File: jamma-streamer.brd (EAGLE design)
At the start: 180.3 x 92 mm, 63 parts, among them IC1 LM7805, J1 Audio line out, J2 ICSP, J3 SDCARD, J4 USB, T1 TY-145P, T2 TY-145P, U1 CD74HC165MD16-M, U10 LM358DTD8-M, U2 ATMEGA328PB-AUR, U3 74HC4050D, U4 TLV757X / LP298X, U5 CD74HC165MD16-M, U6 CD74HC165MD16-M, U7 FT232RL, U8 DS3231SNT&R21-0042B_16-M, U9 NDT2955SOT-223-M, Y1 16MHz

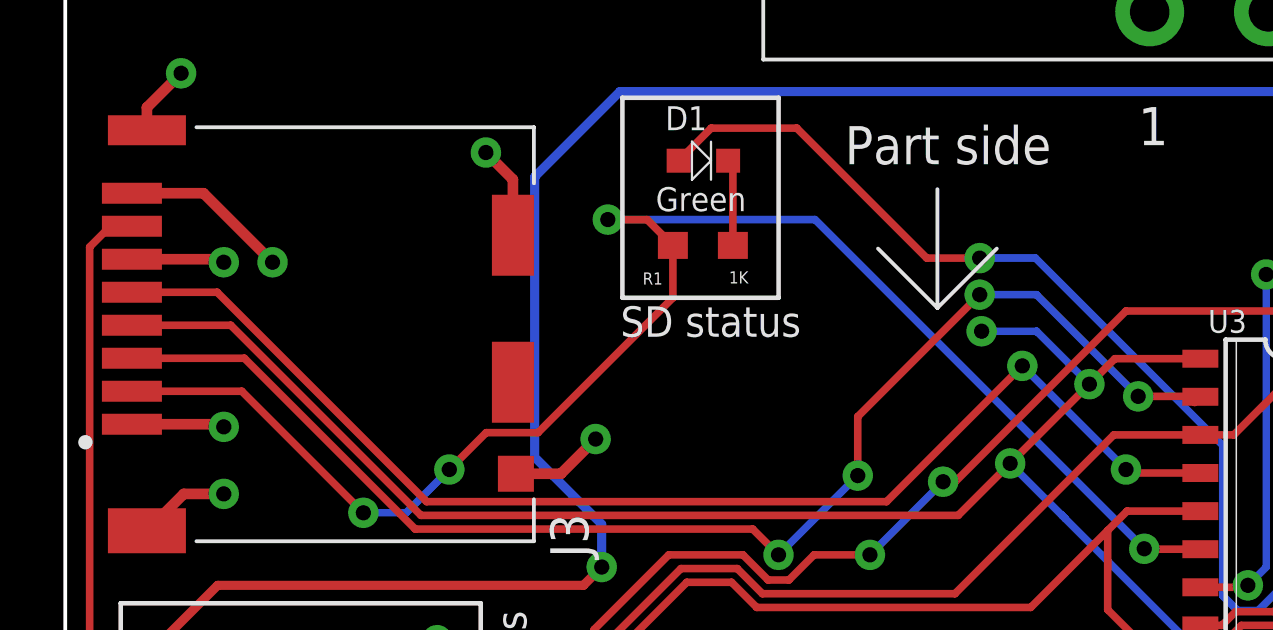
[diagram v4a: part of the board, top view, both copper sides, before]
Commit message: Added Arduino pinout diagram
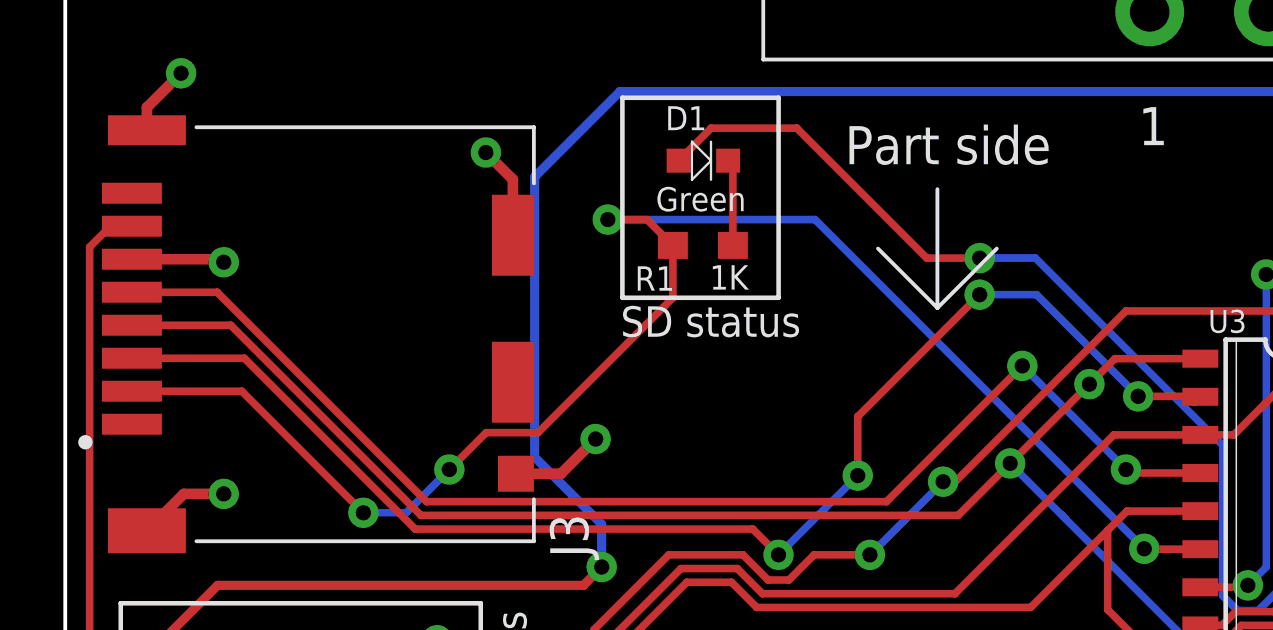
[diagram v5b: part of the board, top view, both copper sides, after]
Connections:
- net N$14 renamed SD_CS
- net N$15 renamed SD_CMD
- net N$17 renamed SD_CLK
- net GND: no longer J3.1, J3.8
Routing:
- net GND: track 221.8 -> 213.0 mm, vias 49 -> 47
- net VCC_2: track 77.9 -> 73.6 mm, vias 6 -> 5
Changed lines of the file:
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@@
 </element>
 <element name="R1" library="CMS" package="652-CHP0603FX1001ELF" value="1K" x="21.25375" y="76.76125" smashed="yes" rot="R180">
-<attribute name="NAME" x="19.91375" y="75.86125" size="0.4064" layer="21" rot="R180"/>
-<attribute name="VALUE" x="22.77125" y="75.8975" size="0.4064" layer="21" rot="R180"/>
+<attribute name="NAME" x="20.32015" y="76.06445" size="0.8128" layer="21" rot="R180"/>
+<attribute name="VALUE" x="22.77125" y="76.1007" size="0.8128" layer="21" rot="R180"/>
 </element>
 <element name="D1" library="CMS" package="604-APTD1608LCGCK" value="Green" x="21.27" y="79.585" smashed="yes">
@@
 </polygon>
 </signal>
-<signal name="GND">
+<signal name="GND" airwireshidden="yes">
 <contactref element="JAMMA_IN" pad="_F"/>
 <contactref element="JAMMA_OUT_BTM" pad="_F"/>
@@
 <contactref element="J3" pad="S2"/>
 <contactref element="J3" pad="6"/>
-<contactref element="J3" pad="8"/>
-<contactref element="J3" pad="1"/>
 <contactref element="U3" pad="8"/>
 <contactref element="U3" pad="11"/>
@@
 <wire x1="3.94965" y1="68.4784" x2="5.2832" y2="68.4784" width="0.3556" layer="1"/>
 <via x="5.2832" y="68.4784" extent="1-16" drill="0.508"/>
-<wire x1="2.22125" y1="70.8" x2="5.1968" y2="70.8" width="0.3556" layer="1"/>
-<wire x1="5.1968" y1="70.8" x2="5.2832" y2="70.7136" width="0.3556" layer="1"/>
-<via x="5.2832" y="70.7136" extent="1-16" drill="0.508"/>
 <wire x1="2.22125" y1="76.3" x2="5.1832" y2="76.3" width="0.3556" layer="1"/>
 <wire x1="5.1832" y1="76.3" x2="5.2832" y2="76.2" width="0.3556" layer="1"/>
 <via x="5.2832" y="76.2" extent="1-16" drill="0.508"/>
-<wire x1="2.22125" y1="78.5" x2="4.6088" y2="78.5" width="0.3556" layer="1"/>
-<wire x1="4.6088" y1="78.5" x2="6.9088" y2="76.2" width="0.3556" layer="1"/>
-<via x="6.9088" y="76.2" extent="1-16" drill="0.508"/>
 <wire x1="2.72125" y1="80.6" x2="2.72125" y2="81.35965" width="0.3556" layer="1"/>
 <wire x1="2.72125" y1="81.35965" x2="3.8608" y2="82.4992" width="0.3556" layer="1"/>
@@
 <wire x1="11.1252" y1="50.7492" x2="9.5504" y2="49.1744" width="0.254" layer="1"/>
 </signal>
-<signal name="N$15">
+<signal name="SD_CMD">
 <contactref element="U3" pad="2"/>
 <contactref element="J3" pad="3"/>
@@
 <wire x1="22.2102375" y1="65.532" x2="20.716625" y2="65.532" width="0.254" layer="1"/>
 </signal>
-<signal name="N$17">
+<signal name="SD_CLK">
 <contactref element="U3" pad="4"/>
 <contactref element="J3" pad="5"/>
@@
 <wire x1="12.0442" y1="68.2198" x2="27.3766" y2="68.2198" width="0.254" layer="1"/>
 </signal>
-<signal name="N$14">
+<signal name="SD_CS">
 <contactref element="J3" pad="2"/>
 <contactref element="U3" pad="6"/>
@@
 <wire x1="34.9866" y1="72.985" x2="34.1376" y2="72.136" width="0.254" layer="1"/>
 <via x="34.1376" y="72.136" extent="1-16" drill="0.508"/>
-<wire x1="34.1376" y1="72.136" x2="32.3736" y2="73.9" width="0.254" layer="16"/>
-<wire x1="32.3736" y1="73.9" x2="30.5448" y2="73.9" width="0.254" layer="16"/>
-<via x="30.5448" y="73.9" extent="1-16" drill="0.508"/>
 <wire x1="34.1376" y1="72.136" x2="31.496" y2="69.4944" width="0.254" layer="1"/>
 <via x="31.496" y="69.4944" extent="1-16" drill="0.508"/>

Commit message: Better routing, elec fixes, doc and sdcard ok
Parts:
- added C14: 0.1uF/16V, CMS:KEMET-C1210C104K4J
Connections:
- net GND: now also C14.2, J3.1, J3.8
- net VCC: now also C14.1
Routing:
- net GND: track 213.0 -> 202.5 mm
- net VCC: track 237.2 -> 247.0 mm, vias 10 -> 12
- net JAMMA+12V: track 104.4 -> 99.6 mm
- net RESET: track 277.6 -> 280.4 mm
- net USBVCC: track 104.7 -> 103.1 mm
- net VCC33: track 72.5 -> 73.5 mm
- net VCC_2: vias 5 -> 4
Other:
- board text added: "Solder to link DTR to ATmega's reset (USB support)"
- board text added: "v0.0.3"
- board text removed: "Solder to link DTR to arduino's reset"
- board text removed: "v0.0.2"

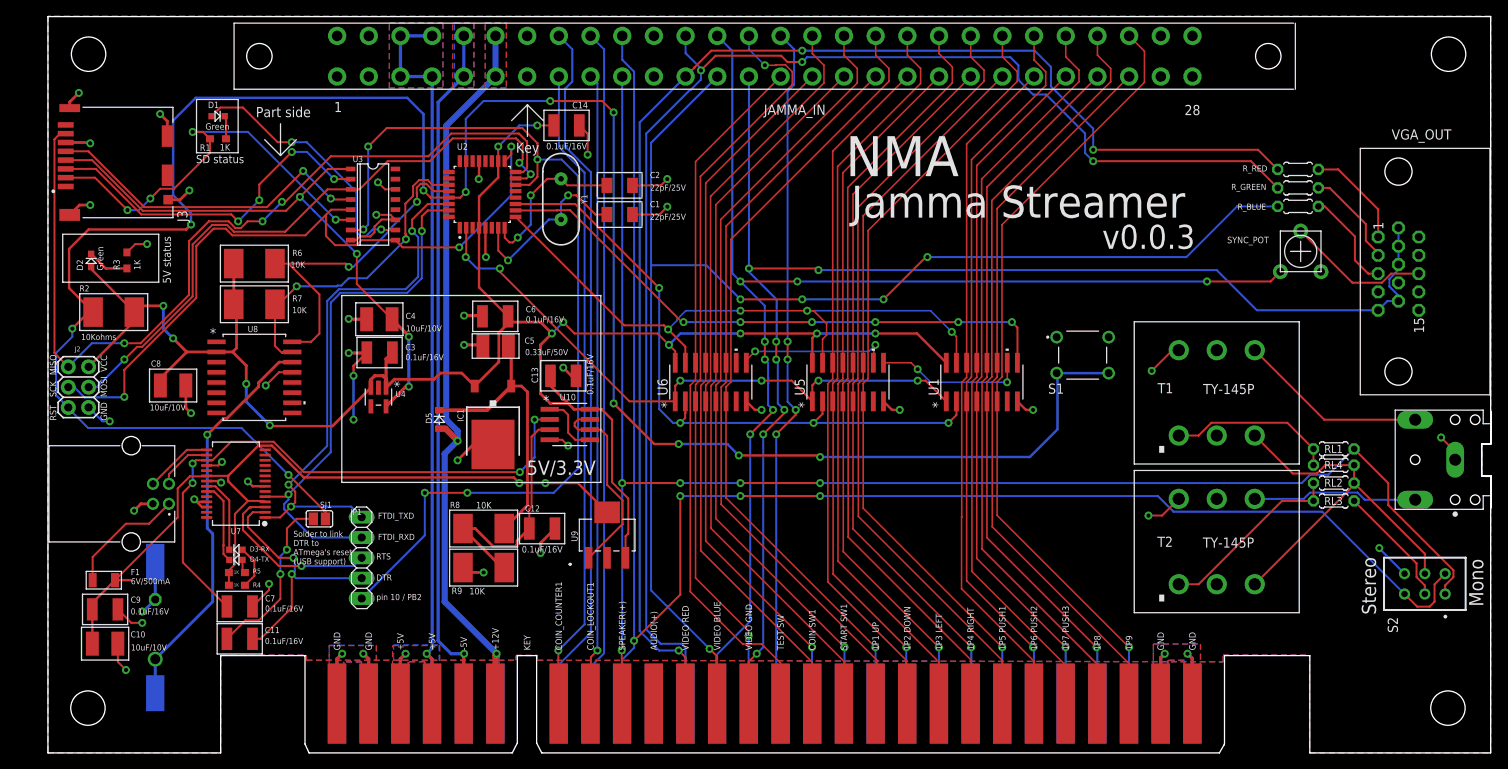
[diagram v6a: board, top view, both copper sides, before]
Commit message: Refacto some parts on the PCB
- new SDCARD slot (push-push): https://www.mouser.fr/ProductDetail/798-DM3AT-SF-PEJM5
- new microUSB connector (type B): https://www.mouser.fr/ProductDetail/806-KMMXBSMT35SB30TR
- resistors replacement for audio (3W) -> need to replace with other
values
- resistors replacement for RGB (SMT)
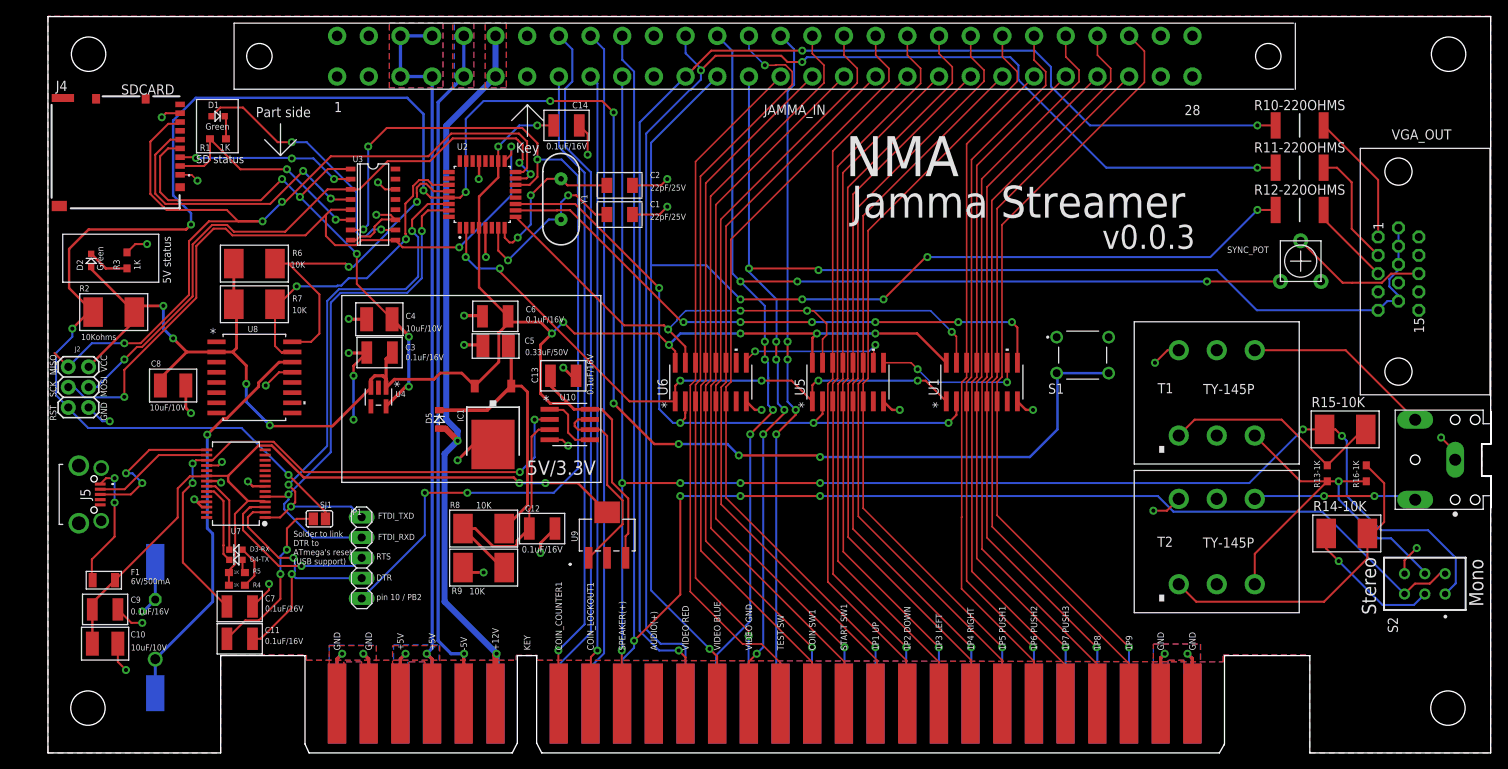
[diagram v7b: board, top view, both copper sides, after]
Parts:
- removed J3: SDCARD, DM3CS-SF:HRS_DM3CS-SF
- removed RL1, RL3: 10K, rcl:0204/5
- removed RL2, RL4: 1K, rcl:0204/5
- removed R_BLUE, R_GREEN, R_RED: 220 ohms, rcl:0204/5
- added J5: KMMX-BSMT35S-B30TR, KMMX-BSMT35S-B30TR:KMMXBSMT35SB30TR
- added R10-220OHMS, R11-220OHMS, R12-220OHMS: CR2512-JW-221ELF, CR2512-JW-221ELF:RESC6331X75N
- added R13-1K, R16-1K: BOURNS-652CHP0603FX1001ELF, CMS:652-CHP0603FX1001ELF
- added R14-10K, R15-10K: BOURNS-CRM2512AJW103ELF, CMS:BOURNS-CRM2512AJW-103ELF
- J4: value USB -> DM3AT-SF-PEJM5; device 292304-1:TE_292304-1 -> DM3AT-SF-PEJM5:DM3AT-SF-PEJM5_1
- moved J4 36.2 mm to (16.5, 68.1)
- moved SYNC_POT 1.22 mm to (156.6, 61.5)
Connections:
- removed net N$24: RL1.2, RL4.1, T1.1
- removed net N$28: RL2.1, RL3.2, T2.1
- removed net N$5: J4.3, U7.15
- removed net N$6: J4.2, U7.16
- removed net N$7: F1.1, J4.1
- new net D+: J5.3, U7.15
- new net D-: J5.2, U7.16
- new net N$11: R13-1K.2, R15-10K.2, T1.1
- new net N$14: R14-10K.2, R16-1K.2, T2.1
- new net USB_V: F1.1, J5.1
- net BLUE: now also R12-220OHMS.1; no longer R_BLUE.1
- net DO: now also J4.7; no longer J3.7
- net GND: now also J4.1, J4.6, J4.8, J5.5, J5.MH1, J5.MH2, J5.MH3, J5.MH4; no longer J3.1, J3.6, J3.8, J3.S1, J3.S2, J3.S3, J3.S5, J4.4
- net GREEN: now also R11-220OHMS.1; no longer R_GREEN.1
- net N$1: now also R10-220OHMS.2; no longer R_RED.2
- net N$16: now also R12-220OHMS.2; no longer R_BLUE.2
- net N$2: now also R11-220OHMS.2; no longer R_GREEN.2
- net N$25: now also R13-1K.1, R16-1K.1; no longer RL2.2, RL4.2
- net N$4: now also R14-10K.1; no longer RL3.1
- net RED: now also R10-220OHMS.1; no longer R_RED.1
- net SD_CLK: now also J4.5; no longer J3.5
- net SD_CMD: now also J4.3; no longer J3.3
- net SD_CS: now also J4.2; no longer J3.2
- net SPK+: now also R15-10K.1; no longer RL1.1
- net VCC_2: now also J4.4; no longer J3.4
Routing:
- net N$14: track 0.00 -> 40.6 mm
- net N$11: track 0.00 -> 28.4 mm
- net N$28: track 23.4 -> 0.00 mm
- net SD_CS: track 51.3 -> 28.6 mm, vias 4 -> 2
- net SD_CMD: track 44.6 -> 22.9 mm, vias 4 -> 3
- net N$24: track 20.9 -> 0.00 mm
- net D+: track 0.00 -> 19.7 mm, vias 0 -> 2
- net USB_V: track 0.00 -> 16.1 mm, vias 0 -> 2
- net N$7: track 15.2 -> 0.00 mm
- net D-: track 0.00 -> 15.1 mm
- net GND: track 202.5 -> 187.6 mm, vias 47 -> 43
- net N$5: track 8.47 -> 0.00 mm
- net N$6: track 6.91 -> 0.00 mm
- net SPK+: track 195.4 -> 201.1 mm, vias 5 -> 7
- net VCC_2: track 73.6 -> 68.3 mm, vias 4 -> 5
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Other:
- board text added: "SDCARD"

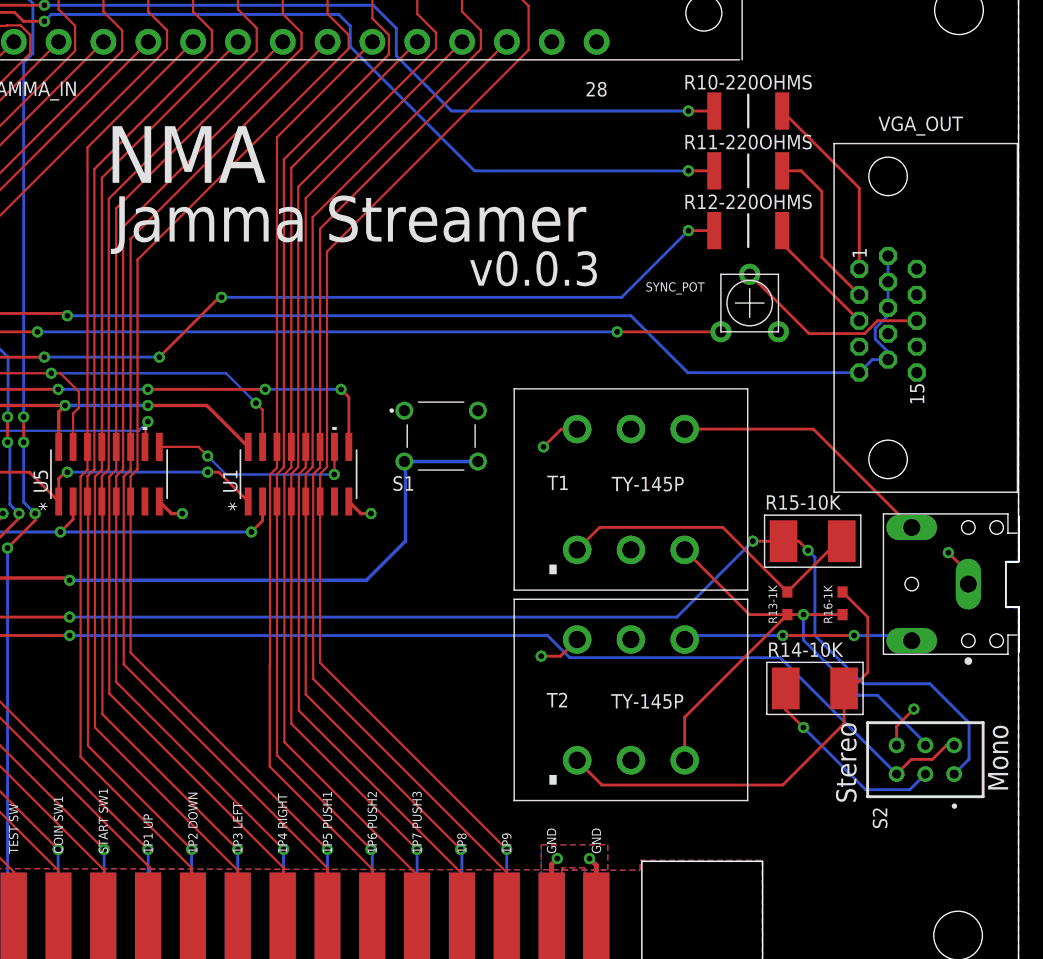
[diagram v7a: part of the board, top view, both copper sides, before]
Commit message: Better resistors for video and audio
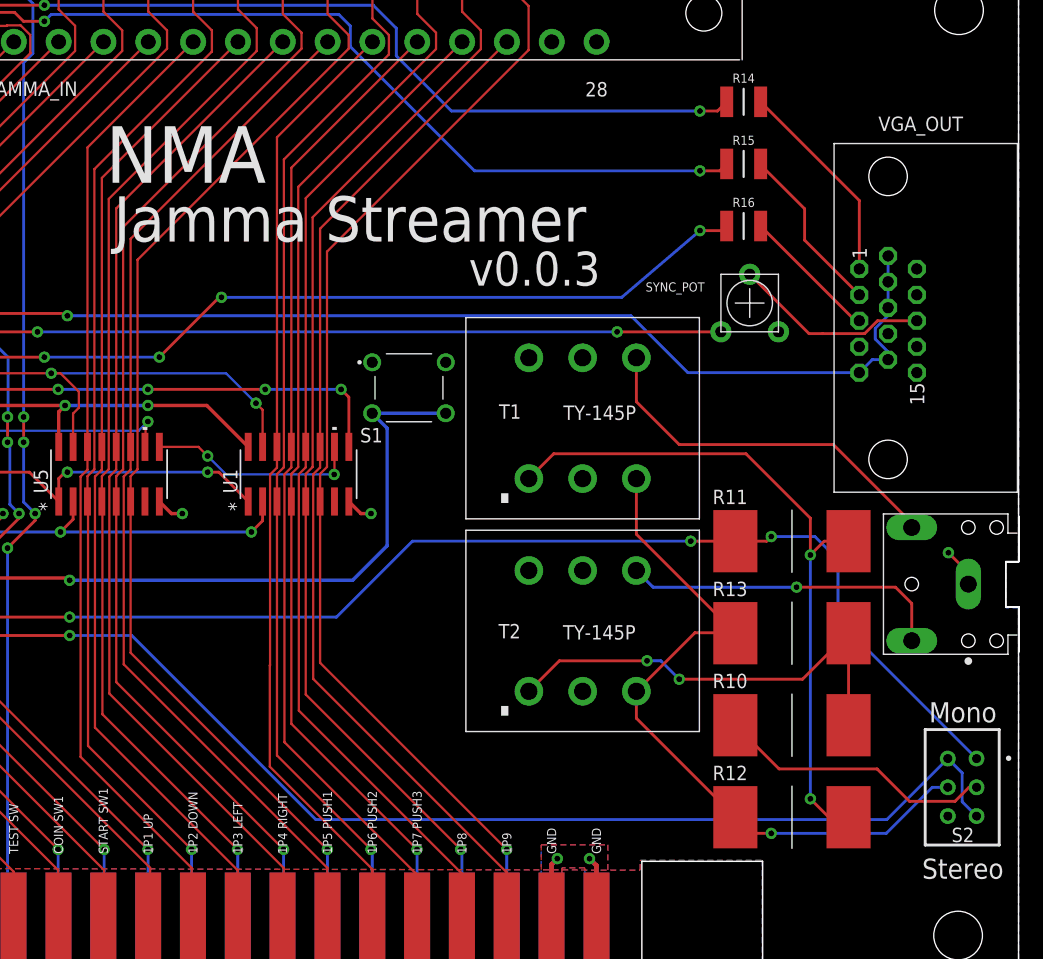
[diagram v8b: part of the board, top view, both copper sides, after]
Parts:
- removed R10-220OHMS, R11-220OHMS, R12-220OHMS: CR2512-JW-221ELF, CR2512-JW-221ELF:RESC6331X75N
- removed R13-1K, R16-1K: BOURNS-652CHP0603FX1001ELF, CMS:652-CHP0603FX1001ELF
- removed R14-10K, R15-10K: BOURNS-CRM2512AJW103ELF, CMS:BOURNS-CRM2512AJW-103ELF
- added R10, R11: 75 ohms, nma-mouser:TE_3550_SERIES
- added R12, R13: 8.2 ohms, nma-mouser:TE_3550_SERIES
- added R14, R15, R16: 220 ohms, nma-mouser:RESC3225X70N
- moved T1 7.61 mm to (141.8, 51.3)
- moved T2 7.44 mm to (141.8, 32.5)
- moved S1 5.13 mm to (126.5, 54.0)
- moved S2 4.06 mm to (175.4, 18.7), turned to 0 degrees
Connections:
- net BLUE: now also R16.1; no longer R12-220OHMS.1
- net GREEN: now also R15.1; no longer R11-220OHMS.1
- net N$1: now also R14.2; no longer R10-220OHMS.2
- net N$11: now also R11.2, R12.2; no longer R13-1K.2, R15-10K.2
- net N$14: now also R10.2, R13.2; no longer R14-10K.2, R16-1K.2
- net N$16: now also R16.2; no longer R12-220OHMS.2
- net N$2: now also R15.2; no longer R11-220OHMS.2
- net N$25: now also R12.1, R13.1; no longer R13-1K.1, R16-1K.1
- net N$4: now also R10.1; no longer R14-10K.1
- net RED: now also R14.1; no longer R10-220OHMS.1
- net SPK+: now also R11.1; no longer R15-10K.1
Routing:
- net N$11: track 28.4 -> 60.8 mm, vias 0 -> 2
- net N$25: track 49.9 -> 63.9 mm
- net GND: track 187.6 -> 176.3 mm, vias 43 -> 40
- net N$26: track 23.7 -> 33.0 mm
- net SPK-: track 207.0 -> 215.4 mm
- net N$30: track 20.4 -> 28.8 mm, vias 2 -> 1
- net N$4: track 17.7 -> 24.6 mm, vias 1 -> 0
- net SPK+: track 201.1 -> 197.5 mm
- net RESET: track 280.4 -> 283.8 mm
- net N$1: track 16.8 -> 18.4 mm
- net RED: track 165.0 -> 166.4 mm
- net N$16: track 10.8 -> 12.2 mm
- net GREEN: track 170.7 -> 172.0 mm
- net BLUE: track 169.7 -> 170.7 mm
- net N$14: track 40.6 -> 39.8 mm, vias 0 -> 2
